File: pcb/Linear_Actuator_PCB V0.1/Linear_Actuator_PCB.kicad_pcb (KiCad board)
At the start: 2 copper layers, 108.5 x 42.9 mm, 45 parts, among them J1 Pwr/Coms, J2 Pot, J3 Bootloader Pins, J5 LED, J7 8P8C, SW1 SW_Push, U1 ATmega328P-AU, Y1 Crystal

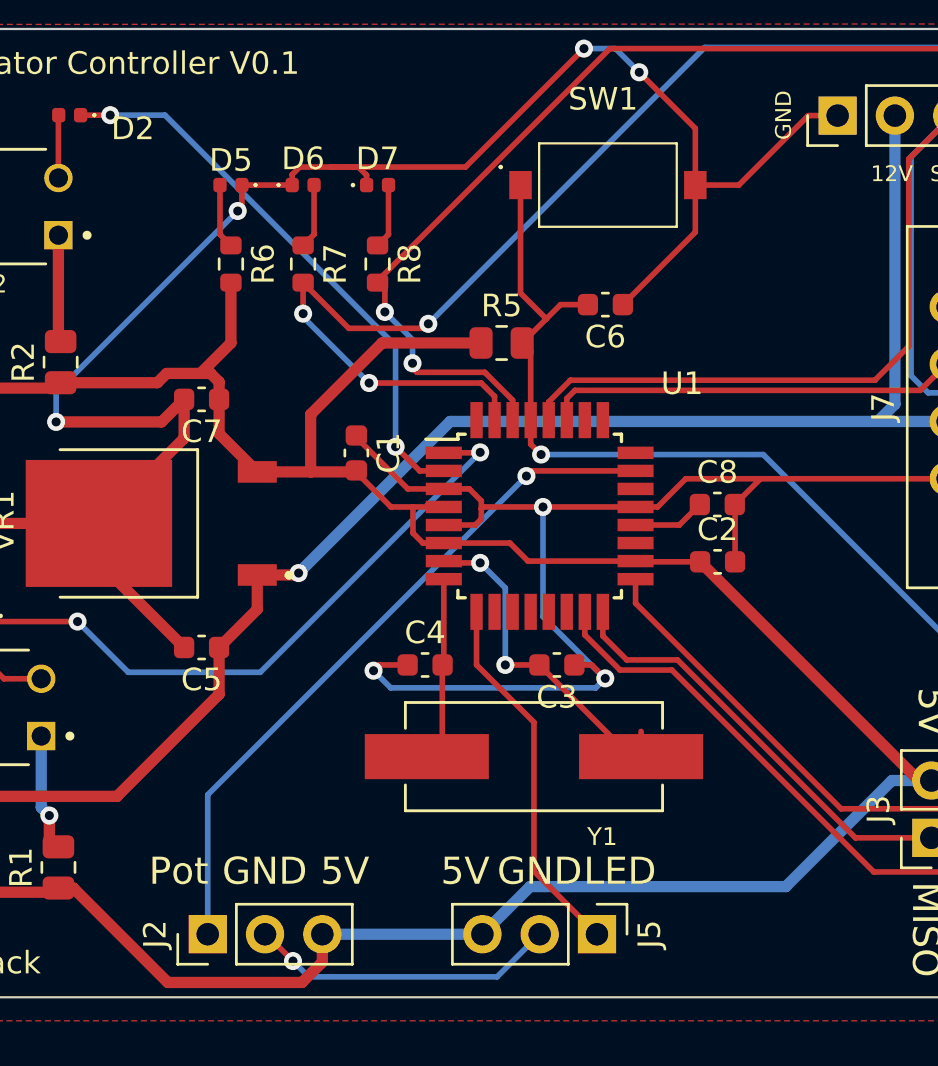
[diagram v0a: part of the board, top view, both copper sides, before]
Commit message: refreshed linear actuator pcb
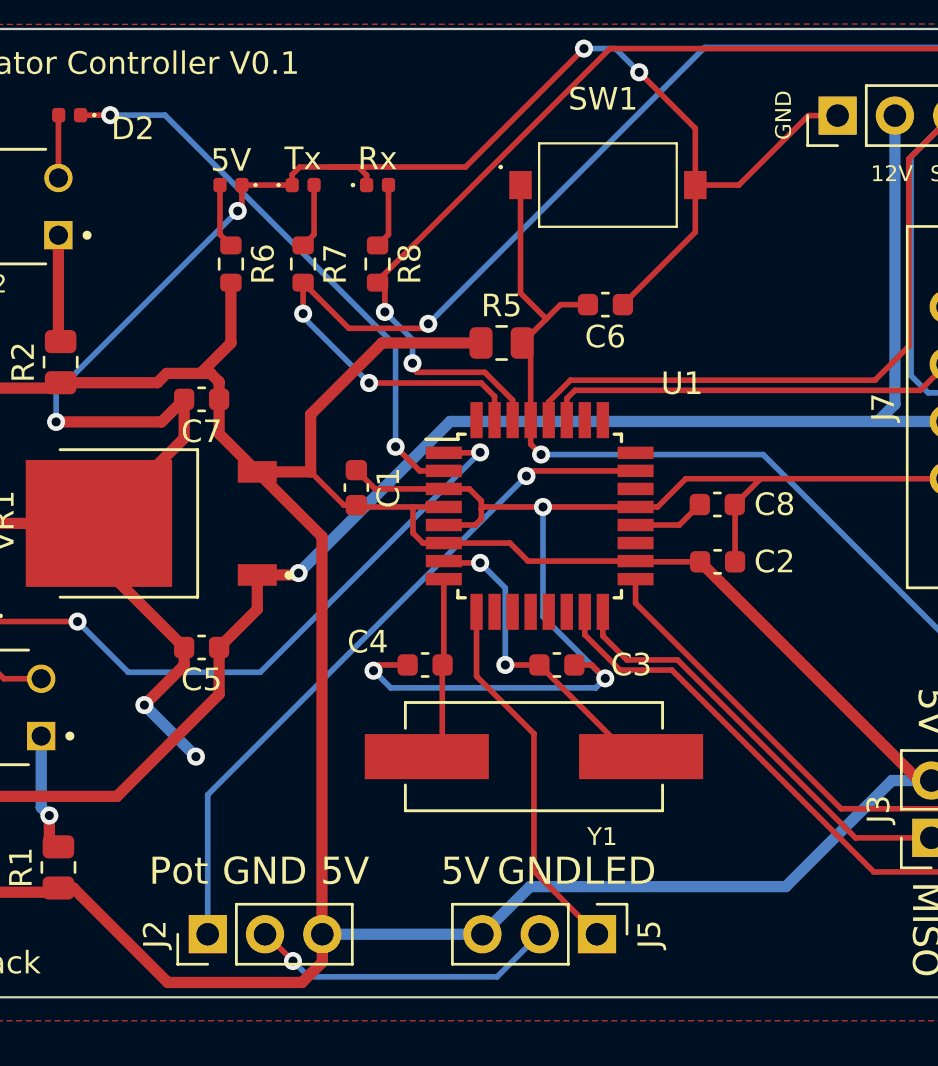
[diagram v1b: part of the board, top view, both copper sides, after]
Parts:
- moved C1 1.54 mm to (162.6, 88.9)
- renumbered D5 to 5V, D7 to Rx, D6 to Tx
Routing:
- net +5V: track 121.5 -> 143.2 mm
- net GND: track 251.7 -> 257.8 mm, vias 8 -> 10
- net Net-(C4-Pad2): track 9.34 -> 8.18 mm
- net Net-(C3-Pad2): track 15.5 -> 14.3 mm

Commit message: New RC control PCB for dirft cart
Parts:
- removed 5V, Rx, Tx: LED, LED_SMD:LED_0402_1005Metric
- removed C1, C2, C6, C8: 100nF, Capacitor_SMD:C_0603_1608Metric
- removed C3, C4: 22pf, Capacitor_SMD:C_0603_1608Metric
- removed C5: 0.33 uF, Capacitor_SMD:C_0603_1608Metric
- removed C7: 0.1uF, Capacitor_SMD:C_0603_1608Metric
- removed SW1: SW_Push, dylan:PTS636SK25SMTRLFS
- removed VR1: LM78M05CDTX_NOPB, dylan:TO228P991X255-3N
- removed Y1: Crystal, dylan:XTAL_ECS-160-20-5PXDN-TR
- added D10: ~, Diode_SMD:D_1210_3225Metric, F.Cu at (308.2, -65.5)
- added D11: ~, Diode_SMD:D_1210_3225Metric, F.Cu at (242.6, -8.10)
- added D12: ~, Diode_SMD:D_1210_3225Metric, F.Cu at (273.3, -28.3)
- added D13: ~, Diode_SMD:D_1210_3225Metric, F.Cu at (277.9, -35.5)
- added D14: LED2, LED_SMD:LED_0402_1005Metric, F.Cu at (298.0, -47.8)
- added D15: LED2, LED_SMD:LED_0402_1005Metric, F.Cu at (263.6, -15.1)
- added D16: LED2, LED_SMD:LED_0402_1005Metric, F.Cu at (308.3, -59.5)
- added D17: LED2, LED_SMD:LED_0402_1005Metric, F.Cu at (263.3, -13.1)
- added D18: ~, Diode_SMD:D_1210_3225Metric, F.Cu at (261.6, -18.2)
- added D19: ~, Diode_SMD:D_1210_3225Metric, F.Cu at (266.9, -25.4)
- added D20: ~, Diode_SMD:D_1210_3225Metric, F.Cu at (258.8, -11.6)
- added D21: ~, Diode_SMD:D_1210_3225Metric, F.Cu at (303.8, -58.4)
- added D22: LED2, LED_SMD:LED_0402_1005Metric, F.Cu at (362.7, -72.5)
- added D23: ~, Diode_SMD:D_1210_3225Metric, F.Cu at (358.2, -71.4)
- added D5: LED, LED_SMD:LED_0402_1005Metric, F.Cu at (319.7, -18.1)
- added D6: LED, LED_SMD:LED_0402_1005Metric, F.Cu at (323.7, -20.7)
- added D7: LED, LED_SMD:LED_0402_1005Metric, F.Cu at (319.7, -16.2)
- added D8: LED2, LED_SMD:LED_0402_1005Metric, F.Cu at (302.4, -52.3)
- added D9: ~, Diode_SMD:D_1210_3225Metric, F.Cu at (287.6, -45.9)
- added F1: 3555-2, dylan:FUSE_3555-2, F.Cu at (327.4, -35.2)
- added F2: 3555-2, dylan:FUSE_3555-2, F.Cu at (327.4, -43.2)
- added J10: BackMotorOutput, Connector_PinSocket_2.54mm:PinSocket_2x06_P2.54mm_Vertical, F.Cu at (270.3, 36.0)
- added J11: ~, Connector_PinHeader_2.54mm:PinHeader_1x02_P2.54mm_Vertical, F.Cu at (242.5, -15.1)
- added J12: ~, Connector_PinHeader_2.54mm:PinHeader_1x02_P2.54mm_Vertical, F.Cu at (247.1, -15.1)
- added J13: ~, Connector_PinHeader_2.54mm:PinHeader_1x02_P2.54mm_Vertical, F.Cu at (256.4, -18.6)
- added J14: ~, Connector_PinHeader_2.54mm:PinHeader_1x02_P2.54mm_Vertical, F.Cu at (251.8, -18.6)
- added J15: ~, Connector_PinHeader_2.54mm:PinHeader_1x02_P2.54mm_Vertical, F.Cu at (261.8, -25.2)
- added J16: ~, Connector_PinHeader_2.54mm:PinHeader_1x02_P2.54mm_Vertical, F.Cu at (282.4, -48.6)
- added J17: ~, Connector_PinHeader_2.54mm:PinHeader_1x02_P2.54mm_Vertical, F.Cu at (303.1, -65.4)
- added J18: ~, Connector_PinHeader_2.54mm:PinHeader_1x02_P2.54mm_Vertical, F.Cu at (292.1, -58.7)
- added J19: ~, Connector_PinHeader_2.54mm:PinHeader_1x02_P2.54mm_Vertical, F.Cu at (272.8, -35.4)
- added J20: 24V IN, dylan:AMASS_XT60PW-M, F.Cu at (98.9, -9.87)
- added J21: 24V IN, dylan:AMASS_XT60PW-M, F.Cu at (158.8, -56.6)
- added J22: 24V Out, dylan:AMASS_XT60PW-M, F.Cu at (144.6, -25.3)
- added J23: 24V Out, dylan:AMASS_XT60PW-M, F.Cu at (161.6, -10.3)
- added J24: 24V Out To DC-DC Converter, dylan:AMASS_XT60PW-M, F.Cu at (81.9, -9.87)
- added J25: 12V IN, dylan:AMASS_XT60PW-M, F.Cu at (127.5, -25.3)
- added J26: 12V OUT Xavier, dylan:AMASS_XT60PW-M, F.Cu at (161.6, -33.5)
- added J27: 12V OUT Router, dylan:AMASS_XT60PW-M, F.Cu at (175.9, -56.6)
- added J28: 12V OUT WaterPump, dylan:AMASS_XT60PW-M, F.Cu at (192.9, -56.6)
- added J29: ~, Connector_PinHeader_2.54mm:PinHeader_1x02_P2.54mm_Vertical, F.Cu at (346.7, -64.6)
- added J9: FrontMotorOutput, Connector_PinSocket_2.54mm:PinSocket_2x06_P2.54mm_Vertical, F.Cu at (289.9, 0.76)
- added K10: 24V 80A E-Stop Relay, dylan:JD2912-1H-24VDC 80A 28VDC, F.Cu at (116.9, 114.4)
- added K11: ~, Relay_THT:Relay_SPDT_Finder_36.11, F.Cu at (326.0, -65.2)
- added K3: ~, Relay_THT:Relay_SPDT_Finder_36.11, F.Cu at (230.1, -42.6)
- added K4: ~, Relay_THT:Relay_SPDT_Finder_36.11, F.Cu at (271.4, -59.3)
- added K5: ~, Relay_THT:Relay_SPDT_Finder_36.11, F.Cu at (230.1, -25.8)
- added K6: ~, Relay_THT:Relay_SPDT_Finder_36.11, F.Cu at (230.1, -59.3)
- added K7: ~, Relay_THT:Relay_SPDT_Finder_36.11, F.Cu at (209.4, -25.8)
- added K8: ~, Relay_THT:Relay_SPDT_Finder_36.11, F.Cu at (250.7, -59.3)
- added K9: ~, Relay_THT:Relay_SPDT_Finder_36.11, F.Cu at (250.7, -42.6)
- added Q10: ~, Package_TO_SOT_THT:TO-92_Inline, F.Cu at (251.4, -10.5)
- added Q11: ~, dylan:DIP762W50P254L650H458Q4B, F.Cu at (265.2, -30.9)
- added Q12: ~, dylan:DIP762W50P254L650H458Q4B, F.Cu at (212.9, -14.1)
- added Q13: ~, dylan:DIP762W50P254L650H458Q4B, F.Cu at (234.9, -14.1)
- added Q14: ~, dylan:DIP762W50P254L650H458Q4B, F.Cu at (274.9, -41.0)
- added Q15: ~, Package_TO_SOT_THT:TO-92_Inline, F.Cu at (222.2, -7.56)
- added Q16: ~, Package_TO_SOT_THT:TO-92_Inline, F.Cu at (228.7, -7.56)
- added Q17: ~, Package_TO_SOT_THT:TO-92_Inline, F.Cu at (209.1, -7.56)
- added Q18: ~, Package_TO_SOT_THT:TO-92_Inline, F.Cu at (215.7, -7.56)
- added Q19: ~, dylan:DIP762W50P254L650H458Q4B, F.Cu at (350.1, -70.2)
- added Q20: ~, Package_TO_SOT_THT:TO-92_Inline, F.Cu at (325.7, -53.5)
- added Q5: ~, dylan:DIP762W50P254L650H458Q4B, F.Cu at (295.5, -64.4)
- added Q6: ~, Package_TO_SOT_THT:TO-92_Inline, F.Cu at (291.7, -50.6)
- added Q7: ~, Package_TO_SOT_THT:TO-92_Inline, F.Cu at (282.1, -40.5)
- added Q8: ~, Package_TO_SOT_THT:TO-92_Inline, F.Cu at (235.2, -7.56)
- added Q9: ~, Package_TO_SOT_THT:TO-92_Inline, F.Cu at (296.4, -57.2)
- added R10: 1K, Resistor_SMD:R_0805_2012Metric, F.Cu at (266.6, -18.9)
- added R11: 1K, Resistor_SMD:R_0805_2012Metric, F.Cu at (313.3, -66.2)
- added R12: 1K, Resistor_SMD:R_0805_2012Metric, F.Cu at (282.9, -33.5)
- added R13: 1K, Resistor_SMD:R_0805_2012Metric, F.Cu at (298.5, -53.2)
- added R14: 1K, Resistor_SMD:R_0805_2012Metric, F.Cu at (288.8, -39.4)
- added R15: 1K, Resistor_SMD:R_0805_2012Metric, F.Cu at (278.3, -29.0)
- added R16: 1K, Resistor_SMD:R_0805_2012Metric, F.Cu at (308.8, -61.9)
- added R17: 1K, Resistor_SMD:R_0805_2012Metric, F.Cu at (288.8, -42.3)
- added R18: 1K, Resistor_SMD:R_0805_2012Metric, F.Cu at (282.9, -36.5)
- added R19: 1K, Resistor_SMD:R_0805_2012Metric, F.Cu at (258.1, -7.97)
- added R20: 1K, Resistor_SMD:R_0805_2012Metric, F.Cu at (266.6, -21.8)
- added R21: 1K, Resistor_SMD:R_0805_2012Metric, F.Cu at (247.6, -6.47)
- added R22: 10k, Resistor_SMD:R_0805_2012Metric, F.Cu at (75.5, 3.59)
- added R23: 15k, Resistor_SMD:R_0805_2012Metric, F.Cu at (80.0, 3.59)
- added R24: 100K, Resistor_SMD:R_0805_2012Metric, F.Cu at (357.5, -45.3)
- added R25: 100K, Resistor_SMD:R_0805_2012Metric, F.Cu at (345.7, -55.3)
- added R26: 100K, Resistor_SMD:R_0805_2012Metric, F.Cu at (351.2, -62.5)
- added R27: 100K, Resistor_SMD:R_0805_2012Metric, F.Cu at (346.6, -58.2)
- added R28: 100K, Resistor_SMD:R_0805_2012Metric, F.Cu at (357.6, -67.8)
- added R29: 100K, Resistor_SMD:R_0805_2012Metric, F.Cu at (341.3, -55.3)
- added R30: 100K, Resistor_SMD:R_0805_2012Metric, F.Cu at (351.2, -65.4)
- added R31: 100K, Resistor_SMD:R_0805_2012Metric, F.Cu at (336.8, -52.4)
- added R32: 100K, Resistor_SMD:R_0805_2012Metric, F.Cu at (341.3, -52.4)
- added R33: 100K, Resistor_SMD:R_0805_2012Metric, F.Cu at (332.4, -52.4)
- added R34: 1K, Resistor_SMD:R_0805_2012Metric, F.Cu at (336.8, -55.3)
- added R35: 1K, Resistor_SMD:R_0805_2012Metric, F.Cu at (332.4, -55.3)
- added R9: 1K, Resistor_SMD:R_0805_2012Metric, F.Cu at (272.0, -24.7)
- added U2: Level Shifter, dylan:CONV_BOB-12009, F.Cu at (262.8, 7.24)
- added U3: RC Pico, dylan:RPi_Pico_SMD_TH, F.Cu at (243.3, 25.0)
- added U4: Autonomous Pico, dylan:RPi_Pico_SMD_TH, F.Cu at (219.2, 25.0)
- added U5: Level Shifter, dylan:CONV_BOB-12009, F.Cu at (262.8, 24.8)
- added U6: 12V TO 5V LM2596 (3A), dylan:DCDC_StepDown_LM2596, F.Cu at (306.7, 144.6)
- added U8: Level Shifter, dylan:CONV_BOB-12009, F.Cu at (277.6, 7.24)
- D1: value LED1 -> LED2
- D3, D4: value ~ -> LED2; footprint Diode_SMD:D_1210_3225Metric -> LED_SMD:LED_0402_1005Metric
- H1, H2, H3, H4: footprint MountingHole:MountingHole_2.2mm_M2 -> MountingHole:MountingHole_5.3mm_M5
- J1: value Pwr/Coms -> RC_PICO_Power/Coms; footprint Connector_PinHeader_2.54mm:PinHeader_1x06_P2.54mm_Vertical -> Connector_PinSocket_2.54mm:PinSocket_2x06_P2.54mm_Vertical_SMD
- J2: value Pot -> FrontServoOutput
- J3: value Bootloader Pins -> RC Reciever; footprint Connector_PinHeader_2.54mm:PinHeader_2x03_P2.54mm_Vertical -> Connector_PinHeader_2.54mm:PinHeader_1x04_P2.54mm_Vertical
- J4: value ~ -> TurretServoOutput_1; footprint Connector_PinHeader_2.54mm:PinHeader_1x02_P2.54mm_Vertical -> Connector_PinHeader_2.54mm:PinHeader_1x03_P2.54mm_Vertical
- J6: value ~ -> TurretServoOutput_2; footprint Connector_PinHeader_2.54mm:PinHeader_1x02_P2.54mm_Vertical -> Connector_PinHeader_2.54mm:PinHeader_1x03_P2.54mm_Vertical
- J7: value 8P8C -> RC_PICO_Power/Coms; footprint Connector_RJ:RJ45_Ninigi_GE -> Connector_PinSocket_2.54mm:PinSocket_2x06_P2.54mm_Vertical
- J8: value ~ -> BackServoOutput; footprint dylan:TE_282837-2 -> Connector_PinHeader_2.54mm:PinHeader_1x03_P2.54mm_Vertical
- Q3, Q4: footprint Package_TO_SOT_THT:TO-92_Inline -> dylan:DIP762W50P254L650H458Q4B
- R5: value 10k -> 1K
- U1: value ATmega328P-AU -> Level Shifter; footprint Package_QFP:TQFP-32_7x7mm_P0.8mm -> dylan:CONV_BOB-12009
- moved H3 231.7 mm to (-7.25, 12.3)
- moved H2 224.8 mm to (-7.40, -4.05)
- moved R1 215.8 mm to (298.5, -50.3), turned to 0 degrees
- moved D2 212.3 mm to (312.7, -63.8), turned to 0 degrees
- moved D3 212.1 mm to (286.4, -50.0), turned to 0 degrees
- moved R4 211.3 mm to (303.1, -54.7), turned to 0 degrees
- moved R3 210.9 mm to (292.6, -46.6), turned to 0 degrees
- moved J2 206.3 mm to (315.7, -21.8), turned to 0 degrees
- moved J8 201.5 mm to (292.1, 18.1), turned to 0 degrees
- moved Q4 193.8 mm to (274.9, -47.6)
- moved R7 192.9 mm to (324.0, -22.9), turned to 0 degrees
- moved R6 192.2 mm to (320.0, -22.9), turned to 0 degrees
- moved J5 189.8 mm to (311.0, -21.8), turned to 0 degrees
- moved R8 185.4 mm to (320.0, -20.4), turned to 0 degrees
- moved Q3 181.9 mm to (254.2, -30.9)
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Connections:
- D1 pad 1: /Relay1 -> /RC_Auto/RC_RelaySig
- D2 pad 1: /Relay2 -> /RC_Auto/RC_RelaySig
- D3 pad 1: Net-(D3-Pad1) -> /RC_Auto/RC_RelaySig
- D4 pad 1: Net-(D4-Pad1) -> /RC_Auto/RC_RelaySig
- J1 pad 1: GND -> +3V3
- J1 pad 2: +12V -> GND
- J1 pad 3: /SCL -> /3.3V_TX
- J1 pad 4: /SDA -> /3.3V_RX
- J1 pad 5: /RXD -> /3.3V_SCL
- J1 pad 6: /TXD -> /3.3V_SDA
- J2 pad 1: /pot -> GND
- J2 pad 2: GND -> /FrontServoOut
- J2 pad 3: +5V -> E-Stop +5V
- J3 pad 1: /MISO -> /5V_Rx
- J3 pad 2: +5V -> /5V_Tx
- J3 pad 3: /SCK -> +5V
- J3 pad 4: /MOSI -> GND
- J4 pad 1: Net-(D3-Pad2) -> GND
- J4 pad 2: +5V -> /TurretServoOut1
- J6 pad 1: Net-(D4-Pad2) -> GND
- J6 pad 2: +5V -> /TurretServoOut2
- J7 pad 1: GND -> +3V3
- J7 pad 3: +12V -> /Auto_3.3V_TX
- J7 pad 4: +12V -> /Auto_3.3V_RX
- J7 pad 5: /SCL -> /Auto_3.3V_SCL
- J7 pad 6: /SDA -> /Auto_3.3V_SDA
- J7 pad 7: /RXD -> /Auto_5V_Tx
- J7 pad 8: /TXD -> /Auto_5V_Rx
- J8 pad 1: Motor- -> GND
- J8 pad 2: Motor+ -> /BackServoOut
- K1 pad 11: Motor- -> /FrontMotorOut
- K1 pad 12: GND -> /3.3V_RC_FrontMotorSig
- K1 pad 14: +12V -> /3.3V_AUTO_FrontMotorSig
- K1 pad A1: Net-(D3-Pad2) -> Net-(D9-Pad2)
- K1 pad A2: Net-(D3-Pad1) -> Net-(D9-Pad1)
- K2 pad 11: Motor+ -> /BackMotorOut
- K2 pad 12: GND -> /3.3V_RC_RearMotorSig
- K2 pad 14: +12V -> /3.3V_AUTO_RearMotorSig
- K2 pad A1: Net-(D4-Pad2) -> Net-(D10-Pad2)
- K2 pad A2: Net-(D4-Pad1) -> Net-(D10-Pad1)
- Q1 pad 4: Net-(D3-Pad2) -> Net-(D9-Pad2)
- Q2 pad 4: Net-(D4-Pad2) -> Net-(D10-Pad2)
- Q3 pad 1: Net-(D3-Pad1) -> Net-(Q3-Pad1)
- Q3 pad 2: Net-(Q3-Pad2) -> Net-(D3-Pad2)
- Q3 pad 3: GND -> Net-(Q3-Pad3)
- Q4 pad 1: Net-(D4-Pad1) -> Net-(Q4-Pad1)
- Q4 pad 2: Net-(Q4-Pad2) -> Net-(D4-Pad2)
- Q4 pad 3: GND -> Net-(Q4-Pad3)
- R3 pad 1: Net-(Q3-Pad2) -> +5V
- R3 pad 2: Net-(Q1-Pad3) -> Net-(Q3-Pad1)
- R4 pad 1: Net-(Q4-Pad2) -> +5V
- R4 pad 2: Net-(Q2-Pad3) -> Net-(Q4-Pad1)
- R5 pad 2: /Reset -> Net-(Q5-Pad1)
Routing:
- net GND: track 257.8 -> 0.00 mm, vias 10 -> 0
- net +5V: track 143.2 -> 0.00 mm
- net +12V: track 128.8 -> 0.00 mm, vias 1 -> 0
- net /TXD: track 69.1 -> 0.00 mm, vias 3 -> 0
- net /RXD: track 58.3 -> 0.00 mm, vias 2 -> 0
- net /Reset: track 48.4 -> 0.00 mm, vias 1 -> 0
- net /SCL: track 45.5 -> 0.00 mm
- net Motor+: track 38.9 -> 0.00 mm
- net Motor-: track 38.5 -> 0.00 mm
- net /pot: track 31.1 -> 0.00 mm, vias 1 -> 0
- net /SDA: track 30.6 -> 0.00 mm
- net Net-(D3-Pad2): track 30.5 -> 0.00 mm
- net Net-(D4-Pad2): track 30.3 -> 0.00 mm
- net /MOSI: track 28.9 -> 0.00 mm
- net /Relay1: track 28.6 -> 0.00 mm, vias 2 -> 0
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- removed copper zone on F.Cu, net GND
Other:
- board size 108.5 x 42.9 mm -> 42.8 x 38.9 mm
- board text removed: "12V"
- board text removed: "5V"
- board text removed: "GND"
- board text removed: "LED"
- board text removed: "MISO"
- board text removed: "MOSI"
- board text removed: "Pot"
- board text removed: "RST"
- board text removed: "Rx"
- board text removed: "SCK"
- board text removed: "SCL"
- board text removed: "SDA"
- board text removed: "Tx"
